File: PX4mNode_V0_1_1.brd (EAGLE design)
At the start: 48.6 x 34.9 mm, 134 parts, among them J201 DF13C-6P-1.25V, J202 DF13C-6P-1.25V, J203 DF13C-6P-1.25V, J301 DF13C-4P-1.25V, J401 DF13C-7P-1.25V, J402 DF13-4P-1.25V, J403 DF13C-4P-1.25V, J404 DF13C-4P-1.25V, J405 DF13C-4P-1.25V, J801 DF13C-3P-1.25V, M3_MOUNT1101 MOUNT-HOLE3.1MM, M3_MOUNT1102 MOUNT-HOLE3.1MM, M3_MOUNT1103 MOUNT-HOLE3.1MM, M3_MOUNT1104 MOUNT-HOLE3.1MM, U101 STM32F4X7VX, U401 MAX3051, U402 MAX3051, X101 3.2x2.5 mm / 24 MHz / 15 ppm

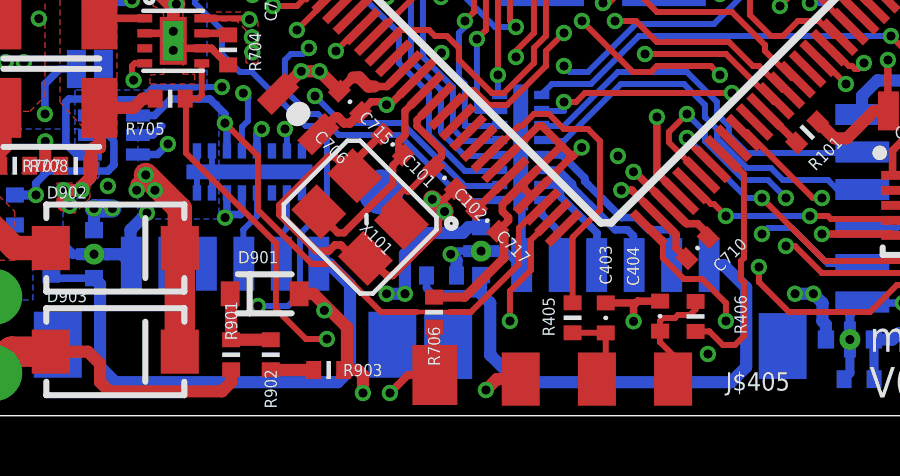
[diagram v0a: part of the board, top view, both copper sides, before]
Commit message: Added schottky diode for VBAT charging
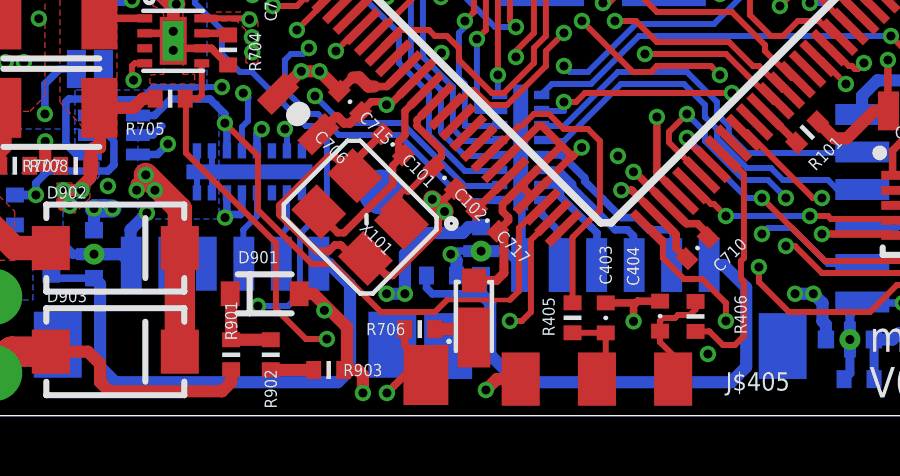
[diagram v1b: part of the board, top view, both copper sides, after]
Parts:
- added D1: MSS1P4-M3, pixhawk2:MICROSMP
- moved R706 0.74 mm to (32.2, 5.63), turned to 0 degrees
- moved JP701 0.30 mm to (32.4, 4.10)
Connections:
- new net N$9: D1.CATHODE, R706.P$2
- net FMU-VDD_3V3: now also D1.ANODE; no longer R706.P$2
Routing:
- net N$9: track 0.00 -> 1.42 mm
- net FMU-VDD_3V3: track 133.4 -> 132.1 mm
- net PPM_INPUT: track 21.0 -> 21.5 mm
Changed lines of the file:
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@@
 <layer number="17" name="Pads" color="2" fill="1" visible="yes" active="yes"/>
 <layer number="18" name="Vias" color="2" fill="1" visible="yes" active="yes"/>
-<layer number="19" name="Unrouted" color="14" fill="1" visible="yes" active="yes"/>
+<layer number="19" name="Unrouted" color="14" fill="1" visible="no" active="yes"/>
 <layer number="20" name="Dimension" color="15" fill="1" visible="yes" active="yes"/>
 <layer number="21" name="tPlace" color="7" fill="1" visible="yes" active="yes"/>
@@
 <attribute name="PARTNO" value="DF13C-4P-1.25V(20)" x="47.0408" y="33.528" size="1.778" layer="28" rot="MR180" display="off"/>
 </element>
-<element name="R706" library="pixhawk2" package="0402-RES" value="1K" x="32.6712" y="6.1944" rot="R90">
-<attribute name="PARTNO" value="RC0402FR-071KL" x="32.6712" y="6.1944" size="1.778" layer="27" rot="R90" display="off"/>
+<element name="R706" library="pixhawk2" package="0402-RES" value="1K" x="32.1944" y="5.6288">
+<attribute name="PARTNO" value="RC0402FR-071KL" x="32.1944" y="5.6288" size="1.778" layer="27" display="off"/>
 </element>
 <element name="C703" library="pixhawk2" package="0402-CAP" value="10n" x="27.2288" y="17.78" rot="R90">
@@
 <attribute name="VALUE" x="40.736853125" y="7.900215625" size="0.4064" layer="27" font="vector" ratio="15" rot="R225"/>
 </element>
-<element name="JP701" library="SparkFun-Connectors" package="PAD-1.5X4.5" value="M01SMD-4.5X1.5" x="32.7" y="4.1"/>
+<element name="JP701" library="SparkFun-Connectors" package="PAD-1.5X4.5" value="M01SMD-4.5X1.5" x="32.4" y="4.1"/>
 <element name="SJ401" library="SparkFun-Passives" package="SJ_2S-NO" value="SOLDERJUMPERNO" x="42.2" y="35.1" rot="R270"/>
 <element name="U$1" library="pixhawk2" package="SOT363_PHILIPS" value="74LVC2GU04" x="22" y="12.1" rot="MR270"/>
@@
 </element>
 <element name="JP4" library="SparkFun-Passives" package="SJ_2S-NO" value="" x="21.2" y="14.3" rot="MR0"/>
+<element name="D1" library="pixhawk2" package="MICROSMP" value="MSS1P4-M3" x="34" y="6.6" rot="R90">
+<attribute name="PARTNO" value="MSS1P4-M3/89A" x="34" y="6.6" size="1.778" layer="27" rot="R90" display="off"/>
+</element>
 </elements>
 <signals>
@@
 <contactref element="R404" pad="P$2"/>
 <contactref element="R402" pad="P$2"/>
-<contactref element="R706" pad="P$2"/>
 <contactref element="U$701" pad="7"/>
 <contactref element="C706" pad="P$1"/>
@@
 <wire x1="25.5" y1="22.8" x2="26.5" y2="21.8" width="0.254" layer="14"/>
 <wire x1="26.5" y1="21.8" x2="27.4" y2="21.8" width="0.254" layer="14"/>
+<contactref element="D1" pad="ANODE"/>
+<wire x1="34.795953125" y1="8.89204375" x2="35" y2="8.687996875" width="0.3048" layer="1"/>
+<wire x1="35" y1="8.687996875" x2="35" y2="7.5" width="0.3048" layer="1"/>
+<wire x1="35" y1="7.5" x2="34.75" y2="7.25" width="0.3048" layer="1"/>
+<wire x1="34.75" y1="7.25" x2="34" y2="7.25" width="0.3048" layer="1"/>
+<wire x1="48.7" y1="26.8" x2="49.2888" y2="26.8208" width="0" layer="19" extent="1-1"/>
+<wire x1="48.6664" y1="18.6944" x2="50.892" y2="21.2344" width="0" layer="19" extent="1-15"/>
+<wire x1="48.9" y1="18" x2="49.22724375" y2="18.13764375" width="0" layer="19" extent="1-1"/>
+<wire x1="49.1504" y1="17.3496" x2="48.572984375" y2="17.483384375" width="0" layer="19" extent="1-15"/>
+<wire x1="42.2" y1="21.8" x2="48.3616" y2="18.6944" width="0" layer="19" extent="1-15"/>
+<wire x1="38.9" y1="28.1" x2="40.3352" y2="21.844" width="0" layer="19" extent="1-16"/>
+<wire x1="38.4016" y1="28.0832" x2="38.4" y2="28.1" width="0" layer="19" extent="1-1"/>
+<wire x1="29.2916" y1="28.332" x2="35.1536" y2="30.988" width="0" layer="19" extent="1-16"/>
 <wire x1="21.8" y1="10.4" x2="21.8" y2="10.9" width="0" layer="19" extent="16-16"/>
-<wire x1="32.6712" y1="6.6944" x2="33.6944" y2="6.6944" width="0.3048" layer="1"/>
-<wire x1="33.6944" y1="6.6944" x2="35" y2="8" width="0.3048" layer="1"/>
-<wire x1="35" y1="8" x2="35" y2="8.687996875" width="0.3048" layer="1"/>
-<wire x1="35" y1="8.687996875" x2="34.795953125" y2="8.89204375" width="0.3048" layer="1"/>
+<wire x1="30.5816" y1="13.208" x2="28.0416" y2="18.8976" width="0" layer="19" extent="1-1"/>
+<wire x1="34.869265625" y1="11.119425" x2="32.0408375" y2="13.94785" width="0" layer="19" extent="1-1"/>
+<wire x1="39.3192" y1="10.8712" x2="37.592" y2="11.684" width="0" layer="19" extent="1-1"/>
 </signal>
 <signal name="OTG_FS_DP">
@@
 <wire x1="51.1048" y1="3.6576" x2="35.8" y2="3.7" width="0.8128" layer="15"/>
 <wire x1="35.8" y1="3.7" x2="34.9" y2="4.6" width="0.8128" layer="15"/>
-<wire x1="34.9" y1="4.6" x2="29.9" y2="4.6" width="0.8128" layer="15"/>
-<wire x1="29.9" y1="4.6" x2="28.9576" y2="3.6576" width="0.8128" layer="15"/>
-<wire x1="28.9576" y1="3.6576" x2="22.352" y2="3.6576" width="0.8128" layer="15"/>
+<wire x1="34.9" y1="4.6" x2="29.8" y2="4.6" width="0.8128" layer="15"/>
+<wire x1="29.8" y1="4.6" x2="28.8576" y2="3.6576" width="0.8128" layer="15"/>
+<wire x1="28.8576" y1="3.6576" x2="22.352" y2="3.6576" width="0.8128" layer="15"/>
 <wire x1="22.352" y1="3.6576" x2="20.32" y2="5.6896" width="0.8128" layer="15"/>
 <wire x1="20.32" y1="5.6896" x2="20.32" y2="10.2616" width="0.8128" layer="15"/>
@@
 <via x="29.4" y="14.9" extent="1-16" drill="0.3" diameter="0.55"/>
 <contactref element="JP701" pad="P$1"/>
-<wire x1="32.7" y1="4.1" x2="31.8" y2="4.1" width="0.254" layer="1"/>
-<wire x1="31.2" y1="3.5" x2="31.8" y2="4.1" width="0.254" layer="1"/>
-<wire x1="29.7" y1="5.8" x2="31.2" y2="4.3" width="0.254" layer="14"/>
-<wire x1="31.2" y1="4.3" x2="31.2" y2="3.5" width="0.254" layer="14"/>
+<wire x1="32.4" y1="4.1" x2="31.7" y2="4.1" width="0.254" layer="1"/>
+<wire x1="31.1" y1="3.5" x2="31.7" y2="4.1" width="0.254" layer="1"/>
+<wire x1="29.7" y1="5.8" x2="31.1" y2="4.4" width="0.254" layer="14"/>
+<wire x1="31.1" y1="4.4" x2="31.1" y2="3.5" width="0.254" layer="14"/>
 <wire x1="29.7" y1="14.6" x2="29.7" y2="5.8" width="0.254" layer="14"/>
 <wire x1="29.4" y1="14.9" x2="29.7" y2="14.6" width="0.254" layer="14"/>
-<via x="31.2" y="3.5" extent="1-16" drill="0.3"/>
-<wire x1="32.6712" y1="5.6944" x2="32.6712" y2="4.1288" width="0.4064" layer="1"/>
-<wire x1="32.6712" y1="4.1288" x2="32.7" y2="4.1" width="0.4064" layer="1"/>
+<via x="31.1" y="3.5" extent="1-16" drill="0.3"/>
+<wire x1="32.6712" y1="4.1288" x2="32.4" y2="4.1" width="0.4064" layer="1"/>
+<wire x1="31.6944" y1="5.6288" x2="31.6944" y2="5.1056" width="0.254" layer="1"/>
+<wire x1="31.6944" y1="5.1056" x2="31.8" y2="5" width="0.254" layer="1"/>
+<wire x1="31.8" y1="5" x2="31.8" y2="4.7" width="0.254" layer="1"/>
+<wire x1="31.8" y1="4.7" x2="32.4" y2="4.1" width="0.254" layer="1"/>
 </signal>
 <signal name="N$11">
@@
 <wire x1="35.2" y1="8.7" x2="32.3" y2="11.6" width="0.2" layer="14"/>
 <wire x1="35.2" y1="5.9" x2="35.2" y2="8.7" width="0.2" layer="14"/>
-<wire x1="35.2" y1="6.9" x2="35.2" y2="5.9" width="0.2" layer="1"/>
-<wire x1="35.9" y1="7.6" x2="35.2" y2="6.9" width="0.2" layer="1"/>
-<wire x1="35.9" y1="8.6" x2="35.9" y2="7.6" width="0.2" layer="1"/>
+<wire x1="35.6" y1="5.9" x2="35.2" y2="5.9" width="0.2" layer="1"/>
+<wire x1="35.9" y1="6.2" x2="35.6" y2="5.9" width="0.2" layer="1"/>
+<wire x1="35.9" y1="8.6" x2="35.9" y2="6.2" width="0.2" layer="1"/>
 <wire x1="36.6" y1="9.3" x2="35.9" y2="8.6" width="0.2" layer="1"/>
 <wire x1="23.1" y1="28.1" x2="23.0632" y2="28.1432" width="0.2" layer="16"/>
@@
 <wire x1="29.3" y1="7.8" x2="28.6" y2="7.8" width="0.2" layer="1"/>
 <wire x1="30.9" y1="6.2" x2="29.3" y2="7.8" width="0.2" layer="1"/>
-<wire x1="33.9" y1="6.2" x2="33.2" y2="6.2" width="0.2" layer="1"/>
-<wire x1="33.2" y1="6.2" x2="32.1" y2="6.2" width="0.154" layer="1"/>
-<wire x1="32.1" y1="6.2" x2="30.9" y2="6.2" width="0.2" layer="1"/>
-<wire x1="35.5" y1="7.8" x2="33.9" y2="6.2" width="0.2" layer="1"/>
-<wire x1="35.5" y1="9" x2="35.5" y2="7.8" width="0.2" layer="1"/>
+<wire x1="33.1" y1="6.6" x2="32.7" y2="6.2" width="0.2" layer="1"/>
+<wire x1="32.7" y1="6.2" x2="30.9" y2="6.2" width="0.2" layer="1"/>
+<wire x1="35.5" y1="6.9" x2="35.2" y2="6.6" width="0.2" layer="1"/>
+<wire x1="35.2" y1="6.6" x2="33.1" y2="6.6" width="0.154" layer="1"/>
+<wire x1="35.5" y1="9" x2="35.5" y2="6.9" width="0.2" layer="1"/>
 <wire x1="36.2" y1="9.7" x2="35.5" y2="9" width="0.2" layer="1"/>
 <wire x1="26.8" y1="11.4" x2="25.6984" y2="12.4952" width="0.2" layer="1"/>
@@
 <wire x1="21.65" y1="13.55" x2="21.65" y2="14.3" width="0.254" layer="16"/>
 </signal>
+<signal name="N$9">
+<contactref element="R706" pad="P$2"/>
+<contactref element="D1" pad="CATHODE"/>
+<wire x1="32.6944" y1="5.6288" x2="33.7212" y2="5.6288" width="0.4064" layer="1"/>
+<wire x1="33.7212" y1="5.6288" x2="34" y2="5.35" width="0.4064" layer="1"/>
+</signal>
 </signals>

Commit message: More untangling
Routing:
- net 5V_S2_FILTERED: track 18.4 -> 0.00 mm
- net !GYRO_CS: track 34.5 -> 32.1 mm, vias 2 -> 3
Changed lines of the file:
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@@
 <layer number="1" name="Top" color="4" fill="1" visible="yes" active="yes"/>
 <layer number="2" name="Ground" color="2" fill="10" visible="no" active="yes"/>
-<layer number="3" name="Horizontal" color="13" fill="15" visible="no" active="yes"/>
+<layer number="3" name="Horizontal" color="13" fill="15" visible="yes" active="yes"/>
 <layer number="4" name="Route4" color="1" fill="4" visible="no" active="no"/>
 <layer number="5" name="Route5" color="4" fill="4" visible="no" active="no"/>
@@
 <layer number="12" name="Route12" color="1" fill="5" visible="no" active="no"/>
 <layer number="13" name="Route13" color="4" fill="5" visible="no" active="no"/>
-<layer number="14" name="Vertical" color="14" fill="15" visible="no" active="yes"/>
-<layer number="15" name="Power" color="11" fill="15" visible="no" active="yes"/>
+<layer number="14" name="Vertical" color="14" fill="15" visible="yes" active="yes"/>
+<layer number="15" name="Power" color="11" fill="15" visible="yes" active="yes"/>
 <layer number="16" name="Bottom" color="1" fill="1" visible="yes" active="yes"/>
 <layer number="17" name="Pads" color="2" fill="1" visible="yes" active="yes"/>
 <layer number="18" name="Vias" color="2" fill="1" visible="yes" active="yes"/>
-<layer number="19" name="Unrouted" color="14" fill="1" visible="no" active="yes"/>
+<layer number="19" name="Unrouted" color="14" fill="1" visible="yes" active="yes"/>
 <layer number="20" name="Dimension" color="15" fill="1" visible="yes" active="yes"/>
 <layer number="21" name="tPlace" color="7" fill="1" visible="yes" active="yes"/>
@@
 <contactref element="U101" pad="7"/>
 <contactref element="U$501" pad="8"/>
-<wire x1="33.2" y1="17.9" x2="30.7" y2="15.4" width="0.2" layer="1"/>
-<wire x1="33.4" y1="17.9" x2="33.2" y2="17.9" width="0.2" layer="1"/>
-<wire x1="33.5" y1="17.8" x2="33.4" y2="17.9" width="0.2" layer="14"/>
-<wire x1="33.5" y1="16.5" x2="33.5" y2="17.8" width="0.2" layer="14"/>
-<wire x1="33.1" y1="16.1" x2="33.5" y2="16.5" width="0.2" layer="14"/>
-<wire x1="33.1" y1="15.4" x2="33.1" y2="16.1" width="0.2" layer="14"/>
-<wire x1="34.2" y1="14.3" x2="33.1" y2="15.4" width="0.2" layer="14"/>
-<wire x1="34.2" y1="12.8" x2="34.2" y2="14.3" width="0.2" layer="14"/>
-<wire x1="41.2" y1="5.8" x2="34.2" y2="12.8" width="0.2" layer="14"/>
-<wire x1="41.2" y1="4.6" x2="41.2" y2="5.8" width="0.2" layer="14"/>
-<wire x1="41.6" y1="4.2" x2="41.2" y2="4.6" width="0.2" layer="14"/>
-<wire x1="42" y1="4.2" x2="41.6" y2="4.2" width="0.2" layer="14"/>
-<wire x1="43.5" y1="5.7" x2="42" y2="4.2" width="0.2" layer="14"/>
-<wire x1="43.5" y1="7.7" x2="43.5" y2="5.7" width="0.2" layer="14"/>
-<wire x1="43.5" y1="7.2" x2="43.5" y2="7.7" width="0.2" layer="1"/>
-<wire x1="44.5" y1="6.2" x2="43.5" y2="7.2" width="0.2" layer="1"/>
-<wire x1="47.2" y1="6.2" x2="44.5" y2="6.2" width="0.2" layer="1"/>
-<wire x1="48.1" y1="7.1" x2="47.2" y2="6.2" width="0.2" layer="1"/>
-<wire x1="30.7" y1="15.4" x2="30.626625" y2="15.362065625" width="0.2" layer="1"/>
-<via x="33.4" y="17.9" extent="1-16" drill="0.3" diameter="0.55"/>
-<via x="43.5" y="7.7" extent="1-16" drill="0.3" diameter="0.55"/>
-<wire x1="48.1" y1="7.1" x2="49.6" y2="7.1" width="0.2" layer="1"/>
-<wire x1="49.6" y1="7.1" x2="49.776" y2="7.276" width="0.2" layer="1"/>
-<wire x1="49.776" y1="7.276" x2="49.776" y2="8.4036" width="0.2" layer="1"/>
+<wire x1="49.776" y1="8.4036" x2="49.776" y2="7.276" width="0.2" layer="1"/>
+<wire x1="49.776" y1="7.276" x2="49.4" y2="6.9" width="0.2" layer="1"/>
+<wire x1="49.4" y1="6.9" x2="49.1" y2="6.9" width="0.2" layer="1"/>
+<via x="49.1" y="6.9" extent="1-16" drill="0.3"/>
+<wire x1="49.1" y1="6.9" x2="46.4" y2="9.6" width="0.2" layer="14"/>
+<wire x1="46.4" y1="9.6" x2="46.4" y2="10.4" width="0.2" layer="14"/>
+<wire x1="46.4" y1="10.4" x2="45.8" y2="11" width="0.2" layer="14"/>
+<wire x1="45.8" y1="11" x2="45.8" y2="16.3" width="0.2" layer="14"/>
+<wire x1="45.8" y1="16.3" x2="45.9" y2="16.4" width="0.2" layer="14"/>
+<wire x1="45.9" y1="16.4" x2="45.9" y2="18.8" width="0.2" layer="14"/>
+<wire x1="45.9" y1="18.8" x2="45.8" y2="18.9" width="0.2" layer="14"/>
+<via x="45.8" y="18.9" extent="1-16" drill="0.3"/>
+<wire x1="45.8" y1="18.9" x2="43.5" y2="18.9" width="0.2" layer="3"/>
+<wire x1="43.5" y1="18.9" x2="42.6" y2="18" width="0.2" layer="3"/>
+<wire x1="42.6" y1="18" x2="33.2" y2="18" width="0.2" layer="3"/>
+<wire x1="33.2" y1="18" x2="33.1" y2="17.9" width="0.2" layer="3"/>
+<via x="33.1" y="17.9" extent="1-16" drill="0.3"/>
+<wire x1="33.1" y1="17.9" x2="33.1" y2="17.835440625" width="0.2" layer="1"/>
+<wire x1="33.1" y1="17.835440625" x2="30.626625" y2="15.362065625" width="0.2" layer="1"/>
 </signal>
 <signal name="SERIAL2_TX">
@@
 <wire x1="29.8" y1="18.4" x2="29.4" y2="18" width="0.2" layer="16"/>
 <wire x1="30.5" y1="18.5" x2="30.3" y2="18.7" width="0.2" layer="3"/>
-<wire x1="33.6" y1="18.5" x2="30.5" y2="18.5" width="0.2" layer="3"/>
-<wire x1="33.8" y1="18.3" x2="33.6" y2="18.5" width="0.2" layer="3"/>
-<wire x1="37.7" y1="18.3" x2="33.8" y2="18.3" width="0.2" layer="3"/>
-<wire x1="37.9" y1="18.5" x2="37.7" y2="18.3" width="0.2" layer="3"/>
-<wire x1="42.2" y1="18.5" x2="37.9" y2="18.5" width="0.2" layer="3"/>
-<wire x1="42.6" y1="18.5" x2="42.2" y2="18.5" width="0.2" layer="1"/>
-<wire x1="45.2" y1="21.1" x2="42.6" y2="18.5" width="0.2" layer="1"/>
+<wire x1="42.4" y1="18.7" x2="42" y2="18.7" width="0.2" layer="3"/>
+<wire x1="42" y1="18.7" x2="41.8" y2="18.5" width="0.2" layer="3"/>
+<wire x1="41.8" y1="18.5" x2="30.5" y2="18.5" width="0.2" layer="3"/>
+<wire x1="42.8" y1="18.7" x2="42.4" y2="18.7" width="0.2" layer="1"/>
+<wire x1="45.2" y1="21.1" x2="42.8" y2="18.7" width="0.2" layer="1"/>
 <wire x1="45.6" y1="21.1" x2="45.2" y2="21.1" width="0.2" layer="1"/>
 <wire x1="46.5" y1="22" x2="45.6" y2="21.1" width="0.2" layer="1"/>
@@
 <wire x1="46.5" y1="22" x2="46.536525" y2="22.079578125" width="0.2" layer="1"/>
 <via x="30.3" y="18.7" extent="1-16" drill="0.3" diameter="0.55"/>
-<via x="42.2" y="18.5" extent="1-16" drill="0.3" diameter="0.55"/>
+<via x="42.4" y="18.7" extent="1-16" drill="0.3" diameter="0.55"/>
 </signal>
 <signal name="FMU-USART3_CTS">
@@
 <contactref element="L204" pad="P$2"/>
 <contactref element="U$203" pad="C"/>
-<wire x1="34.544" y1="6.5024" x2="34.544" y2="4.7672" width="0.4064" layer="16"/>
-<wire x1="34.544" y1="4.7672" x2="35.4504" y2="3.8608" width="0.4064" layer="16"/>
-<wire x1="35.4504" y1="3.8608" x2="42.5704" y2="3.8608" width="0.4064" layer="16"/>
-<wire x1="42.5704" y1="3.8608" x2="43.0752" y2="4.3656" width="0.4064" layer="16"/>
-<wire x1="43.0752" y1="4.3656" x2="43.0752" y2="7.0136" width="0.4064" layer="16"/>
-<wire x1="43.0752" y1="7.0136" x2="42.3248" y2="7.764" width="0.4064" layer="16"/>
-<wire x1="42.3248" y1="7.764" x2="41.841" y2="7.764" width="0.4064" layer="16"/>
-<wire x1="34.544" y1="6.5024" x2="34.2392" y2="6.8072" width="0.4064" layer="16"/>
-<wire x1="34.2392" y1="6.8072" x2="34.2392" y2="7.4296" width="0.4064" layer="16"/>
-<wire x1="32.4184" y1="7.4168" x2="32.4184" y2="7.0024" width="0.254" layer="16"/>
-<wire x1="32.4184" y1="7.0024" x2="32.6136" y2="6.8072" width="0.254" layer="16"/>
-<wire x1="32.6136" y1="6.8072" x2="34.2392" y2="6.8072" width="0.254" layer="16"/>
+<wire x1="34.2392" y1="7.4296" x2="41.841" y2="7.764" width="0" layer="19" extent="16-16"/>
+<wire x1="32.4184" y1="7.4168" x2="34.2392" y2="7.4296" width="0" layer="19" extent="16-16"/>
 </signal>
 <signal name="FMU-!RESET">
